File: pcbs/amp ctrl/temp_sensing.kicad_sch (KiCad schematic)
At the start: 8 parts

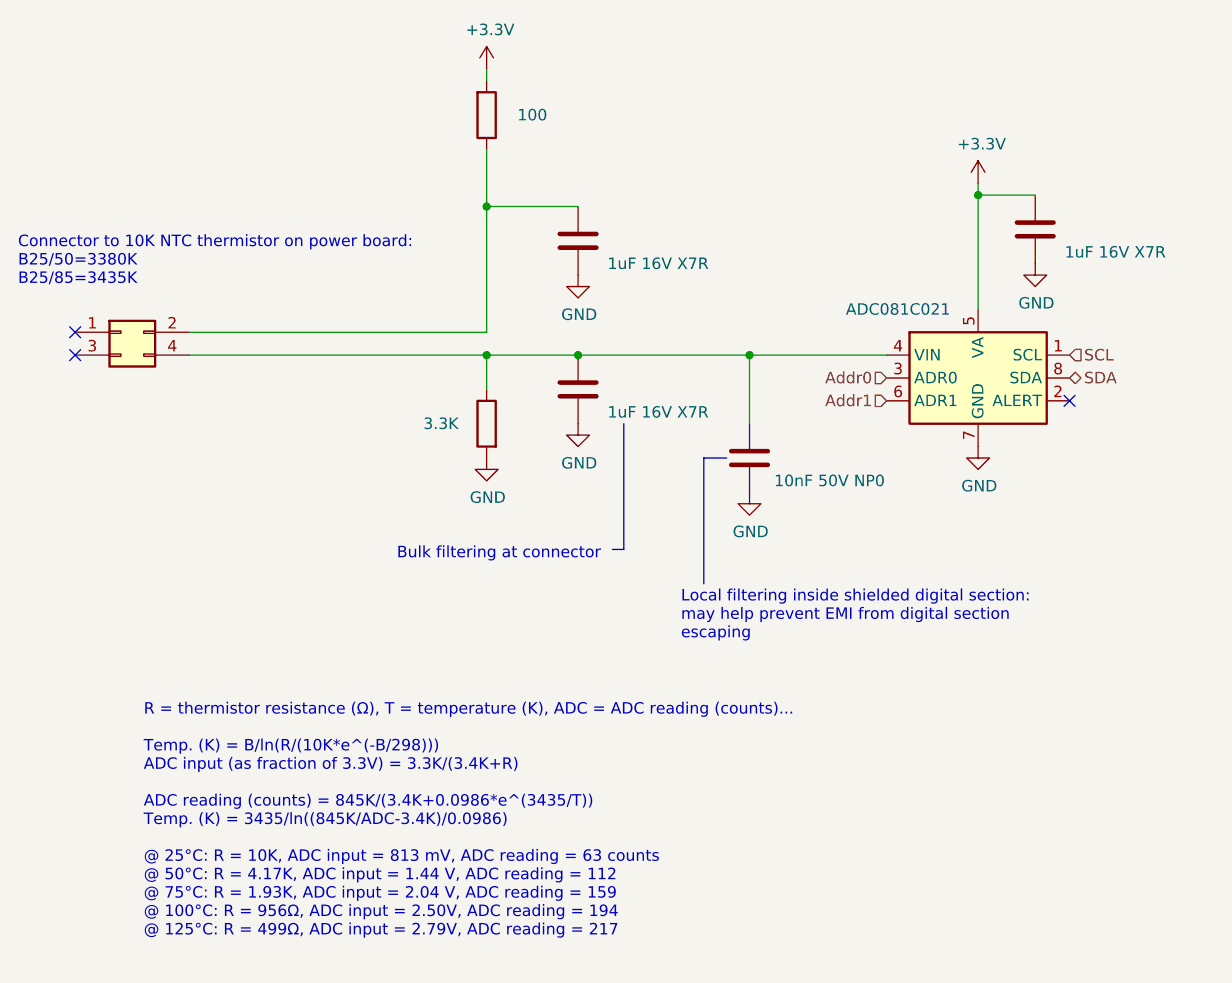
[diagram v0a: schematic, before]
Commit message: Schematic file fix, misc. PCB
Fixed issue with KiCAD's automatic V5→V6 migration (corrected in 6.0.11) that caused problems with component references in multi-channel schematic sheets
Finished migration in amp ctrl PCB, inc. re-assigning "exclude from BOM" attributes to testpoints, solder jumpers
Added mounting hole to amp ctrl PCB for addl support to Ethernet jacks, power connector through stiffener
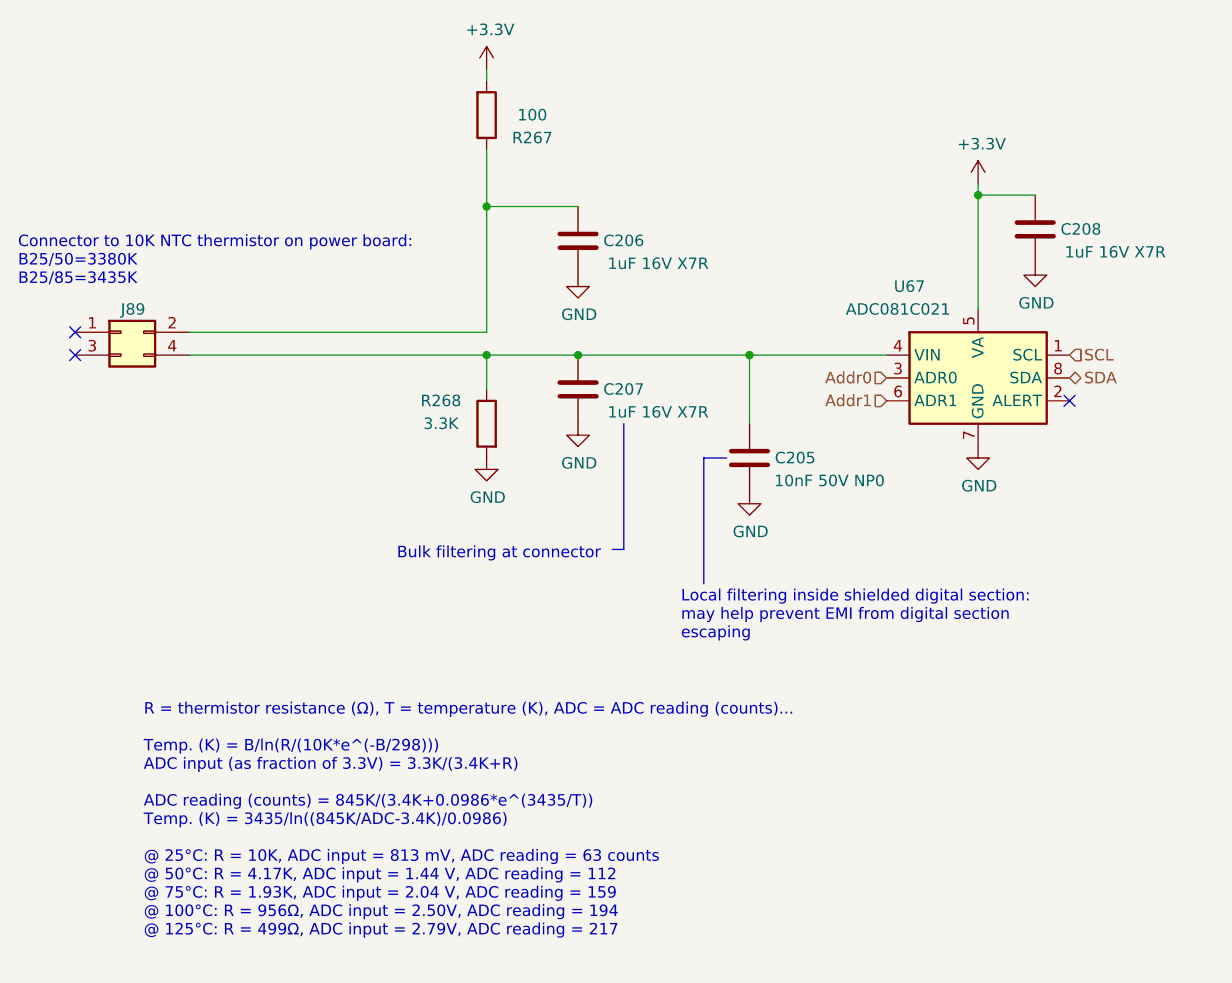
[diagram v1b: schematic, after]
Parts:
- gave numbers to parts that had none: 8

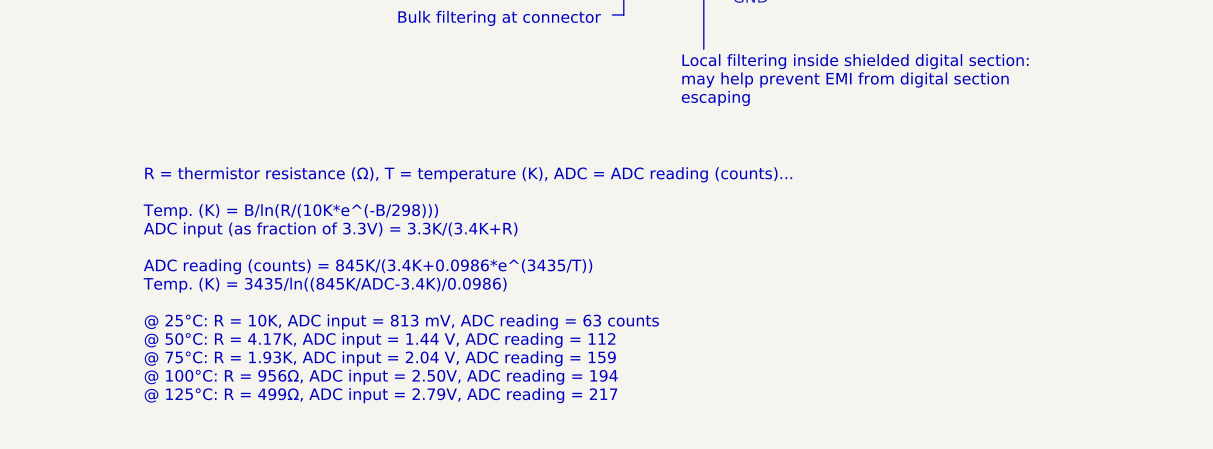
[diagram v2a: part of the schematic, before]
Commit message: Upgraded to KiCAD 7.0 format Added 10µF cap to ADC's REFP pins to fix the voltage reference output (#15) Corrected ADC & DAC reset by adding a separate reset circuit (#14) Increased Cfbk compensation cap on each channel to work out-of-the-box with small coils (#16)
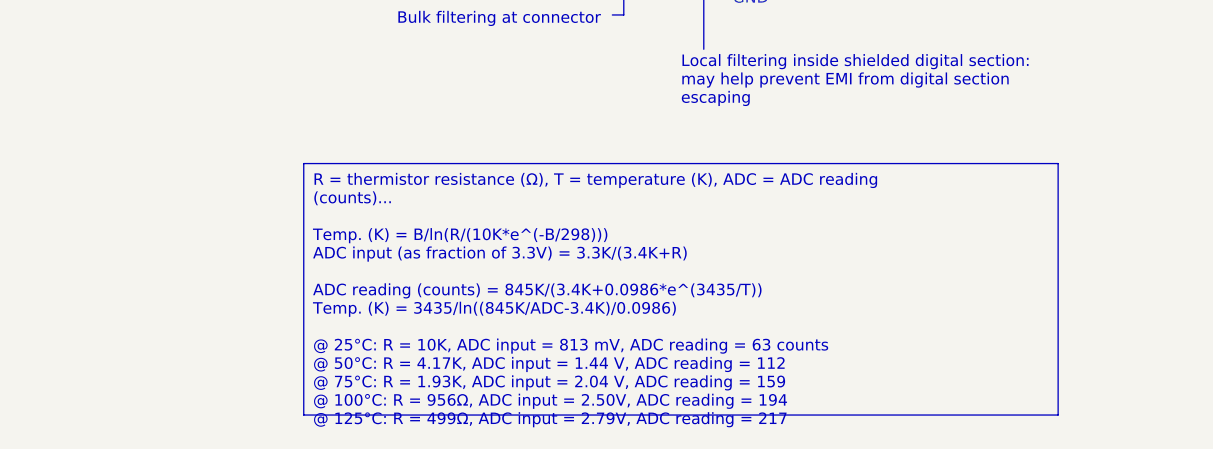
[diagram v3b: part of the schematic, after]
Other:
- note removed: "R = thermistor resistance (Ω), T = temperature (K), ADC = ADC reading (counts)... Temp. (K) = B/ln(R/(10K*e^(-B/298))) ADC input (as fraction of 3.3V) = 3.3K/(3.4K+R) ADC reading (counts) = 845K/(3.4K+0.0986*e^(3435/T)) Temp. (K) = 3435/ln((845K/ADC-3.4K)/0.0986) @ 25°C: R = 10K, ADC input = 813 mV, ADC reading = 63 counts @ 50°C: R = 4.17K, ADC input = 1.44 V, ADC reading = 112 @ 75°C: R = 1.93K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"

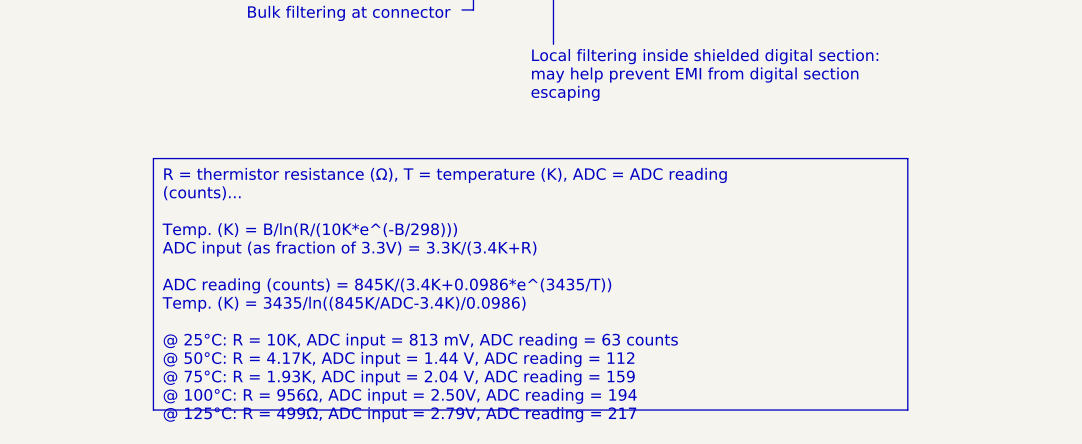
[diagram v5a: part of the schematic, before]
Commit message: Updated KiCAD file versions to 9.0
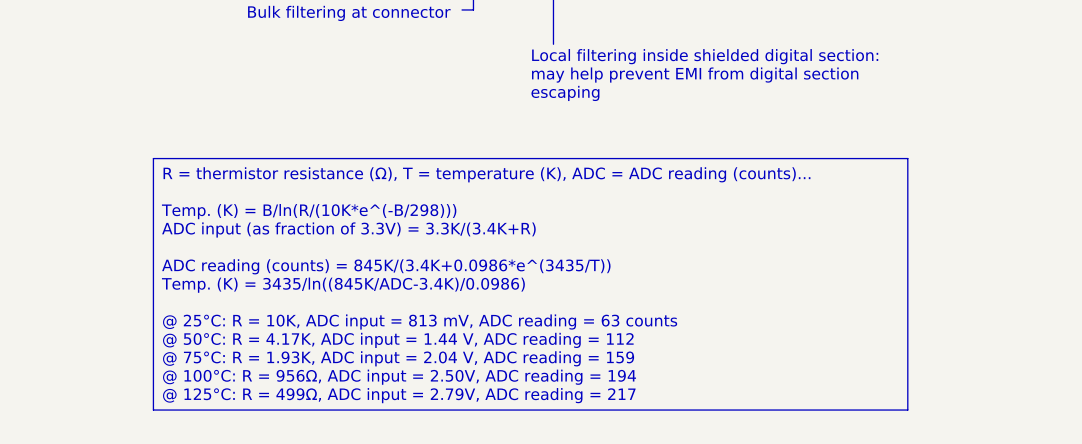
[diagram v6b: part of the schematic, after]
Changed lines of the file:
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@@
 (kicad_sch
-	(version 20231120)
+	(version 20250114)
 	(generator "eeschema")
-	(generator_version "8.0")
+	(generator_version "9.0")
 	(paper "A4")
 	(title_block
@@
 		(comment 1 "Don Straney")
 	)
-	(junction
-		(at 127 78.74)
-		(diameter 0)
-		(color 0 0 0 0)
-	)
-	(junction
-		(at 181.61 77.47)
-		(diameter 0)
-		(color 0 0 0 0)
-	)
-	(junction
-		(at 137.16 95.25)
-		(diameter 0)
-		(color 0 0 0 0)
-	)
-	(junction
-		(at 127 95.25)
-		(diameter 0)
-		(color 0 0 0 0)
-	)
-	(junction
-		(at 156.21 95.25)
-		(diameter 0)
-		(color 0 0 0 0)
-	)
-	(no_connect
-		(at 81.28 92.71)
-	)
-	(no_connect
-		(at 191.77 100.33)
-	)
-	(no_connect
-		(at 81.28 95.25)
-	)
-	(polyline
-		(pts
-			(xy 151.13 106.68) (xy 153.67 106.68)
-		)
-		(stroke
-			(width 0)
-			(type default)
-		)
-	)
-	(wire
-		(pts
-			(xy 181.61 77.47) (xy 181.61 90.17)
-		)
-		(stroke
-			(width 0)
-			(type default)
-		)
-	)
-	(wire
-		(pts
-			(xy 93.98 92.71) (xy 127 92.71)
-		)
-		(stroke
-			(width 0)
-			(type default)
-		)
-	)
-	(polyline
-		(pts
-			(xy 142.24 116.84) (xy 140.97 116.84)
-		)
-		(stroke
-			(width 0)
-			(type default)
-		)
-	)
-	(wire
-		(pts
-			(xy 137.16 78.74) (xy 127 78.74)
-		)
-		(stroke
-			(width 0)
-			(type default)
-		)
-	)
-	(wire
-		(pts
-			(xy 127 72.39) (xy 127 78.74)
-		)
-		(stroke
-			(width 0)
-			(type default)
-		)
-	)
-	(wire
-		(pts
-			(xy 137.16 95.25) (xy 156.21 95.25)
-		)
-		(stroke
-			(width 0)
-			(type default)
-		)
-	)
-	(polyline
-		(pts
-			(xy 151.13 120.65) (xy 151.13 106.68)
-		)
-		(stroke
-			(width 0)
-			(type default)
-		)
-	)
-	(wire
-		(pts
-			(xy 187.96 77.47) (xy 181.61 77.47)
-		)
-		(stroke
-			(width 0)
-			(type default)
-		)
-	)
-	(wire
-		(pts
-			(xy 127 95.25) (xy 137.16 95.25)
-		)
-		(stroke
-			(width 0)
-			(type default)
-		)
-	)
-	(wire
-		(pts
-			(xy 93.98 95.25) (xy 127 95.25)
-		)
-		(stroke
-			(width 0)
-			(type default)
-		)
-	)
-	(wire
-		(pts
-			(xy 156.21 102.87) (xy 156.21 95.25)
-		)
-		(stroke
-			(width 0)
-			(type default)
-		)
-	)
-	(wire
-		(pts
-			(xy 127 95.25) (xy 127 99.06)
-		)
-		(stroke
-			(width 0)
-			(type default)
-		)
-	)
-	(wire
-		(pts
-			(xy 181.61 77.47) (xy 181.61 76.2)
-		)
-		(stroke
-			(width 0)
-			(type default)
-		)
-	)
-	(polyline
-		(pts
-			(xy 142.24 102.87) (xy 142.24 116.84)
-		)
-		(stroke
-			(width 0)
-			(type default)
-		)
-	)
-	(wire
-		(pts
-			(xy 127 78.74) (xy 127 92.71)
-		)
-		(stroke
-			(width 0)
-			(type default)
-		)
-	)
-	(wire
-		(pts
-			(xy 156.21 95.25) (xy 171.45 95.25)
-		)
-		(stroke
-			(width 0)
-			(type default)
-		)
-	)
-	(wire
-		(pts
-			(xy 127 64.77) (xy 127 63.5)
-		)
-		(stroke
-			(width 0)
-			(type default)
+	(text "Connector to 10K NTC thermistor on power board:\nB25/50=3380K\nB25/85=3435K"
+		(exclude_from_sim no)
+		(at 74.93 87.63 0)
+		(effects
+			(font
+				(size 1.27 1.27)
+			)
+			(justify left bottom)
+		)
+	)
+	(text "Bulk filtering at connector"
+		(exclude_from_sim no)
+		(at 139.7 118.11 0)
+		(effects
+			(font
+				(size 1.27 1.27)
+			)
+			(justify right bottom)
+		)
+	)
+	(text "Local filtering inside shielded digital section:\nmay help prevent EMI from digital section\nescaping"
+		(exclude_from_sim no)
+		(at 148.59 127 0)
+		(effects
+			(font
+				(size 1.27 1.27)
+			)
+			(justify left bottom)
 		)
 	)
@@
 		(at 106.68 133.35 0)
 		(size 83.82 27.94)
+		(margins 0.9525 0.9525 0.9525 0.9525)
 		(stroke
 			(width 0)
@@
 		)
 	)
-	(text "Connector to 10K NTC thermistor on power board:\nB25/50=3380K\nB25/85=3435K"
-		(exclude_from_sim no)
-		(at 74.93 87.63 0)
-		(effects
-			(font
-				(size 1.27 1.27)
-			)
-			(justify left bottom)
-		)
-	)
-	(text "Bulk filtering at connector"
-		(exclude_from_sim no)
-		(at 139.7 118.11 0)
-		(effects
-			(font
-				(size 1.27 1.27)
-			)
-			(justify right bottom)
-		)
-	)
-	(text "Local filtering inside shielded digital section:\nmay help prevent EMI from digital section\nescaping"
-		(exclude_from_sim no)
-		(at 148.59 127 0)
-		(effects
-			(font
-				(size 1.27 1.27)
-			)
-			(justify left bottom)
-		)
-	)
+	(junction
+		(at 127 78.74)
+		(diameter 0)
+		(color 0 0 0 0)
+	)
+	(junction
+		(at 181.61 77.47)
+		(diameter 0)
+		(color 0 0 0 0)
+	)
+	(junction
+		(at 137.16 95.25)
+		(diameter 0)
+		(color 0 0 0 0)
+	)
+	(junction
+		(at 127 95.25)
+		(diameter 0)
+		(color 0 0 0 0)
+	)
+	(junction
+		(at 156.21 95.25)
+		(diameter 0)
+		(color 0 0 0 0)
+	)
+	(no_connect
+		(at 81.28 92.71)
+	)
+	(no_connect
+		(at 191.77 100.33)
+	)
+	(no_connect
+		(at 81.28 95.25)
+	)
+	(polyline
+		(pts
+			(xy 151.13 106.68) (xy 153.67 106.68)
+		)
+		(stroke
+			(width 0)
+			(type default)
+		)
+	)
+	(wire
+		(pts
+			(xy 181.61 77.47) (xy 181.61 90.17)
+		)
+		(stroke
+			(width 0)
+			(type default)
+		)
+	)
+	(wire
+		(pts
+			(xy 93.98 92.71) (xy 127 92.71)
+		)
+		(stroke
+			(width 0)
+			(type default)
+		)
+	)
+	(polyline
+		(pts
+			(xy 142.24 116.84) (xy 140.97 116.84)
+		)
+		(stroke
+			(width 0)
+			(type default)
+		)
+	)
+	(wire
+		(pts
+			(xy 137.16 78.74) (xy 127 78.74)
+		)
+		(stroke
+			(width 0)
+			(type default)
+		)
+	)
+	(wire
+		(pts
+			(xy 127 72.39) (xy 127 78.74)
+		)
+		(stroke
+			(width 0)
+			(type default)
+		)
+	)
+	(wire
+		(pts
+			(xy 137.16 95.25) (xy 156.21 95.25)
+		)
+		(stroke
+			(width 0)
+			(type default)
+		)
+	)
+	(polyline
+		(pts
+			(xy 151.13 120.65) (xy 151.13 106.68)
+		)
+		(stroke
+			(width 0)
+			(type default)
+		)
+	)
+	(wire
+		(pts
+			(xy 187.96 77.47) (xy 181.61 77.47)
+		)
+		(stroke
+			(width 0)
+			(type default)
+		)
+	)
+	(wire
+		(pts
+			(xy 127 95.25) (xy 137.16 95.25)
+		)
+		(stroke
+			(width 0)
+			(type default)
+		)
+	)
+	(wire
+		(pts
+			(xy 93.98 95.25) (xy 127 95.25)
+		)
+		(stroke
+			(width 0)
+			(type default)
+		)
+	)
+	(wire
+		(pts
+			(xy 156.21 102.87) (xy 156.21 95.25)
+		)
+		(stroke
+			(width 0)
+			(type default)
+		)
+	)
+	(wire
+		(pts
+			(xy 127 95.25) (xy 127 99.06)
+		)
+		(stroke
+			(width 0)
+			(type default)
+		)
+	)
+	(wire
+		(pts
+			(xy 181.61 77.47) (xy 181.61 76.2)
+		)
+		(stroke
+			(width 0)
+			(type default)
+		)
+	)
+	(polyline
+		(pts
+			(xy 142.24 102.87) (xy 142.24 116.84)
+		)
+		(stroke
+			(width 0)
+			(type default)
+		)
+	)
+	(wire
+		(pts
+			(xy 127 78.74) (xy 127 92.71)
+		)
+		(stroke
+			(width 0)
+			(type default)
+		)
+	)
+	(wire
+		(pts
+			(xy 156.21 95.25) (xy 171.45 95.25)
+		)
+		(stroke
+			(width 0)
+			(type default)
+		)
+	)
+	(wire
+		(pts
+			(xy 127 64.77) (xy 127 63.5)
+		)
+		(stroke
+			(width 0)
+			(type default)
+		)
+	)

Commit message: Moved all project-specific symbols & footprints into new "shim" libraries Updated projects to reference the new "shim" library
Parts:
- J89: footprint Martinos:PinSocket_2x02_P2.54mm_Vertical_SMD_BotEntry_Pin -> shim:PinSocket_2x02_P2.54mm_Vertical_SMD_BotEntry_Pin
- U67: footprint Martinos_std:MSOP-8_3x3mm_P0.65mm -> Package_SO:MSOP-8_3x3mm_P0.65mm
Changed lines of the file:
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@@
 			)
 		)
-		(property "Footprint" "Martinos:PinSocket_2x02_P2.54mm_Vertical_SMD_BotEntry_Pin"
+		(property "Footprint" "shim:PinSocket_2x02_P2.54mm_Vertical_SMD_BotEntry_Pin"
 			(at 86.36 92.71 0)
 			(effects
@@
 			)
 		)
-		(property "Footprint" "Martinos_std:MSOP-8_3x3mm_P0.65mm"
+		(property "Footprint" "Package_SO:MSOP-8_3x3mm_P0.65mm"
 			(at 201.93 106.68 0)
 			(effects

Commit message: BOM & reset fixes
Amp ctrl: changed name of "Manufacturer" field to "MPN" to work with Aisler
Amp ctrl: added part number to logic inverter, corrected various typos and part number problems
Backplane: added pull-down to Shutdown_Reset signal (#35)
Backplane: rethought Shutdown_Force circuit to make fail-safe (broken connections->shutdown), make work correctly (fixes #35)
Backplane: updated/corrected various schematic annotations
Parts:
- C205: MPN (none) -> GRM1885C1H103JA01D; Part Number GRM1885C1H103JA01D -> (none)
- C206, C207, C208: MPN (none) -> C0603C105K4RACTU; Part Number C0603C105K4RACTU -> (none)
- J89: MPN (none) -> M20-7810245 / M20-7810245R; MPN Alt. (none) -> HLE-102-02-L-DV / HLE-102-02-F-DV / HLE-102-02-G-DV / HLE-1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; Part Number M20-7810245 / M20-7810245R -> (none); Part Number Alt. HLE-102-02-L-DV / HLE-102-02-F-DV / HLE-102-02-G-DV / HLE-1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 -> (none)
- R267: MPN (none) -> RK73H2ATTD1000F; Part Number RK73H2ATTD1000F -> (none)
- R268: MPN (none) -> RK73H2ATTD3301F; Part Number RK73H2ATTD3301F -> (none)
- U67: MPN (none) -> ADC081C021CIMM/NOPB; Part Number ADC081C021CIMM/NOPB -> (none)
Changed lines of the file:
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@@
 			)
 		)
-		(property "Part Number" "GRM1885C1H103JA01D"
+		(property "MPN" "GRM1885C1H103JA01D"
 			(at 156.21 106.68 0)
 			(effects
@@
 			)
 		)
-		(property "Part Number" "M20-7810245 / M20-7810245R"
+		(property "Notes" ""
 			(at 86.36 92.71 0)
 			(effects
@@
 			)
 		)
-		(property "Part Number Alt." "HLE-102-02-L-DV / HLE-102-02-F-DV / HLE-102-02-G-DV / HLE-102-02-S-DV / HLE-102-02-SM-DV / HLE-102-02-H-DV"
+		(property "MPN" "M20-7810245 / M20-7810245R"
 			(at 86.36 92.71 0)
 			(effects
@@
 			)
 		)
-		(property "Notes" ""
+		(property "MPN Alt." "HLE-102-02-L-DV / HLE-102-02-F-DV / HLE-102-02-G-DV / HLE-102-02-S-DV / HLE-102-02-SM-DV / HLE-102-02-H-DV"
 			(at 86.36 92.71 0)
 			(effects
@@
 			)
 		)
-		(property "Part Number" "RK73H2ATTD3301F"
+		(property "MPN" "RK73H2ATTD3301F"
 			(at 127 102.87 0)
 			(effects
@@
 			)
 		)
-		(property "Part Number" "C0603C105K4RACTU"
+		(property "Type" "SMT"
 			(at 137.16 99.06 0)
 			(effects
@@
 			)
 		)
-		(property "Type" "SMT"
+		(property "MPN" "C0603C105K4RACTU"
 			(at 137.16 99.06 0)
 			(effects
@@
 			)
 		)
-		(property "Part Number" "RK73H2ATTD1000F"
+		(property "MPN" "RK73H2ATTD1000F"
 			(at 127 68.58 0)
 			(effects
@@
 			)
 		)
-		(property "Part Number" "C0603C105K4RACTU"
+		(property "Type" "SMT"
 			(at 137.16 82.55 0)
 			(effects
@@
 			)
 		)
-		(property "Type" "SMT"
+		(property "MPN" "C0603C105K4RACTU"
 			(at 137.16 82.55 0)
 			(effects
@@
 			)
 		)
-		(property "Part Number" "C0603C105K4RACTU"
-			(at 187.96 81.28 0)
-			(effects
-				(font
-					(size 1.27 1.27)
-				)
-				(hide yes)
-			)
-		)
 		(property "Type" "SMT"
 			(at 187.96 81.28 0)
@@
 			)
 		)
+		(property "MPN" "C0603C105K4RACTU"
+			(at 187.96 81.28 0)
+			(effects
+				(font
+					(size 1.27 1.27)
+				)
+				(hide yes)
+			)
+		)
 		(pin "1"
 		)
@@
 			)
 		)
-		(property "Part Number" "ADC081C021CIMM/NOPB"
-			(at 181.61 97.79 0)
-			(effects
-				(font
-					(size 1.27 1.27)
-				)
-				(hide yes)
-			)
-		)
 		(property "Type" "SMT"
 			(at 181.61 97.79 0)
 			(effects
+				(font
+					(size 1.27 1.27)
+				)
+				(hide yes)
+			)
+		)
+		(property "MPN" "ADC081C021CIMM/NOPB"
+			(at 181.61 97.79 0)
+			(effects
